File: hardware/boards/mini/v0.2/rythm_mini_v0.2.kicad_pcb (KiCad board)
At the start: 8 copper layers, 18 x 50 mm, 73 parts, among them IC1 NAU88C22YG, IC2 IS42S32160F-6BLI, Q1 PMV37EN22, U1 W25Q128JVP, U2 LTV-217-G, U4 STM32H750XBHx, Y1 Crystal_GND24

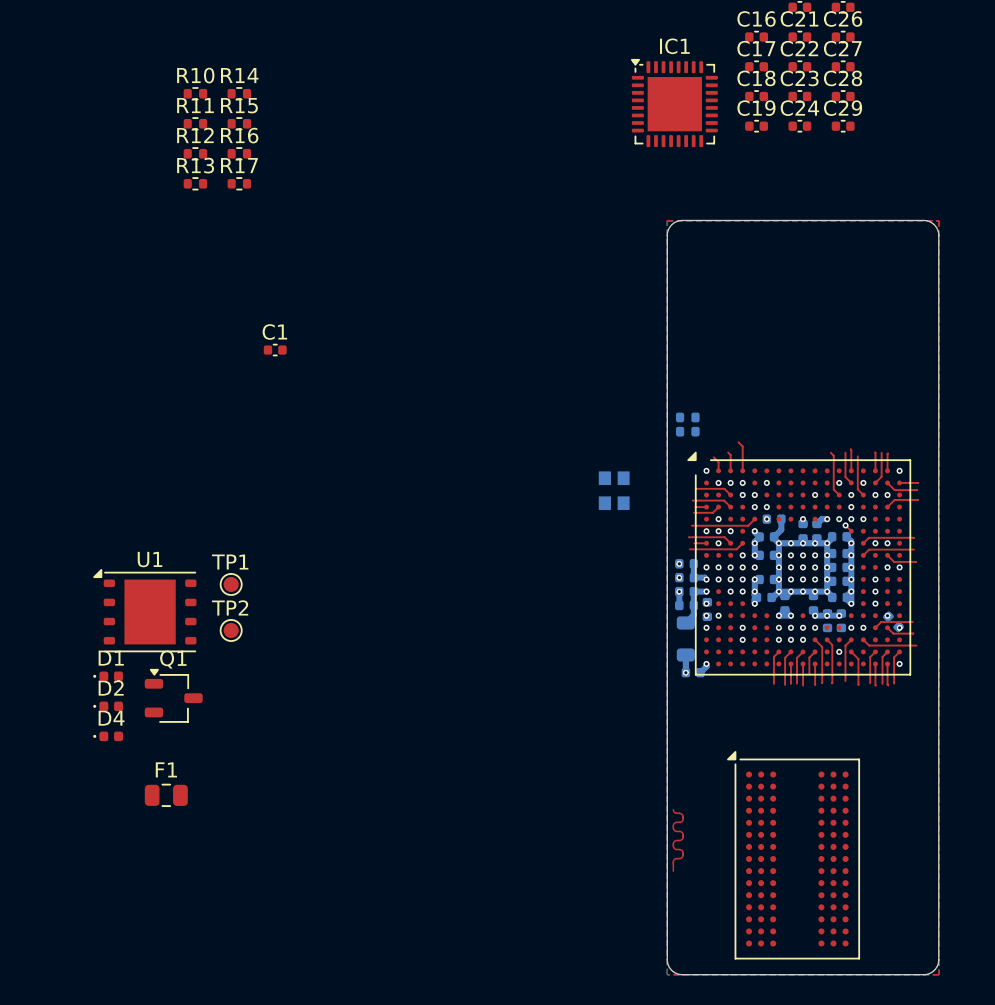
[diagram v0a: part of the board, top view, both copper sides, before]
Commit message: place stm32h750 decoupling capacitors
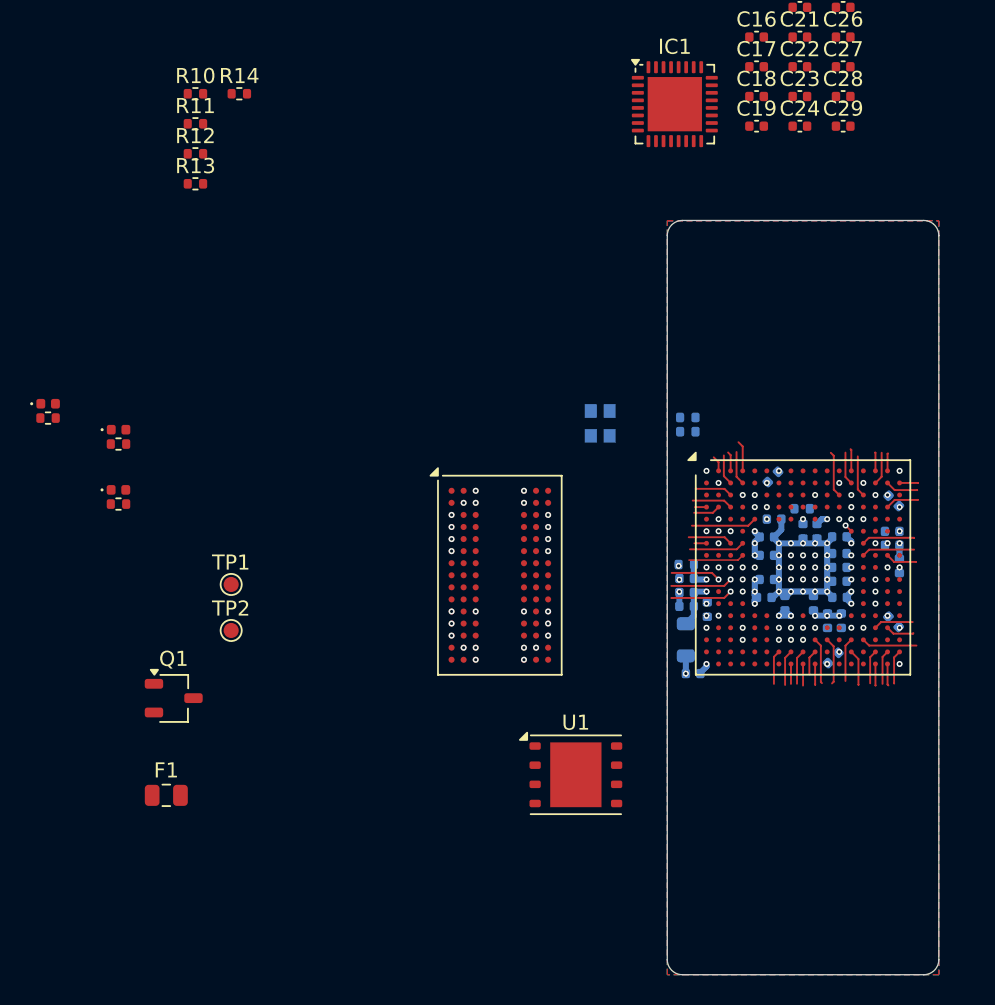
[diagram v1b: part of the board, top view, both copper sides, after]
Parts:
- added C2: 2.2 uF <100 mΩ ESR, Capacitor_SMD:C_0402_1005Metric, B.Cu at (86.0, 73.6)
- added C3: 2.2 uF <100 mΩ ESR, Capacitor_SMD:C_0402_1005Metric, B.Cu at (78.0, 72.0)
- added C4: 1uF 600mΩ, Capacitor_SMD:C_0402_1005Metric, B.Cu at (85.9, 75.6)
- added C5: 100nF, Capacitor_SMD:C_0402_1005Metric, B.Cu at (85.9, 76.5)
- added C6: 1uF, Capacitor_SMD:C_0402_1005Metric, B.Cu at (86.4, 77.9)
- added R18: 10k, Resistor_SMD:R_0402_1005Metric, B.Cu at (79.9, 74.1)
- C1: moved to B.Cu
- R5: value 4.7k -> 10k; footprint Capacitor_SMD:C_0402_1005Metric -> Resistor_SMD:R_0402_1005Metric
- moved C1 42.2 mm to (82.0, 84.0), turned to 45 degrees
- moved U1 30.2 mm to (64.9, 91.7)
- moved IC2 27.3 mm to (59.9, 78.5)
- moved R17 22.7 mm to (34.6, 73.8)
- moved R15 22.7 mm to (34.6, 69.8)
- moved R16 21.6 mm to (29.9, 68.1)
- moved D1 18.5 mm to (30.0, 67.2)
- moved D2 18.3 mm to (34.6, 68.9)
- moved D4 16.3 mm to (34.6, 72.9)
- moved Y1 4.56 mm to (66.6, 68.5)
- moved C31 0.06 mm to (72.3, 80.6)
- moved C30 0.06 mm to (72.3, 79.7)
- moved C32 0.06 mm to (72.7, 85.0)
- moved C33 0.06 mm to (72.3, 78.7)
- moved FB1 0.06 mm to (72.2, 82.8)
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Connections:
- C1 pad 1: unconnected-(C1-Pad1) -> Net-(C1-Pad1)
- C1 pad 2: unconnected-(C1-Pad2) -> GND
- U4 pad A7: unconnected-(U4L-VCAP-PadA7) -> Net-(C3-Pad1)
- U4 pad D17: unconnected-(U4L-VCAP-PadD17) -> Net-(C2-Pad1)
- U4 pad E7: unconnected-(U4L-PDR_ON-PadE7) -> +3.3V
- U4 pad E8: unconnected-(U4L-BOOT0-PadE8) -> /BOOT0
- U4 pad F17: unconnected-(U4L-VDD33_USB-PadF17) -> +3.3V
- U4 pad G17: unconnected-(U4L-VDD50_USB-PadG17) -> +3.3V
- U4 pad U11: unconnected-(U4L-VCAP-PadU11) -> Net-(C1-Pad1)
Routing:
- net +3.3V: track 17.3 -> 35.9 mm, vias 23 -> 39
- net /FMC_A4: track 0.00 -> 5.41 mm
- net /FMC_A5: track 0.00 -> 4.78 mm
- net /FMC_D6: track 0.00 -> 4.44 mm
- net /FMC_D8: track 0.00 -> 4.32 mm
- net /QSPI_CLK: track 0.00 -> 4.11 mm
- net /QSPI_IO2: track 0.00 -> 4.11 mm
- net /FMC_A7: track 0.00 -> 3.97 mm
- net /FMC_A8: track 0.00 -> 3.96 mm
- net /I2C_SCL: track 0.00 -> 3.96 mm
- net /FMC_A3: track 0.00 -> 3.70 mm, vias 1 -> 0
- net /FMC_A6: track 0.00 -> 3.63 mm
- net /I2C_SDA: track 0.00 -> 3.50 mm
- net /QSPI_IO3: track 6.62 -> 3.29 mm
- net /FMC_NBL0: track 0.00 -> 3.31 mm
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
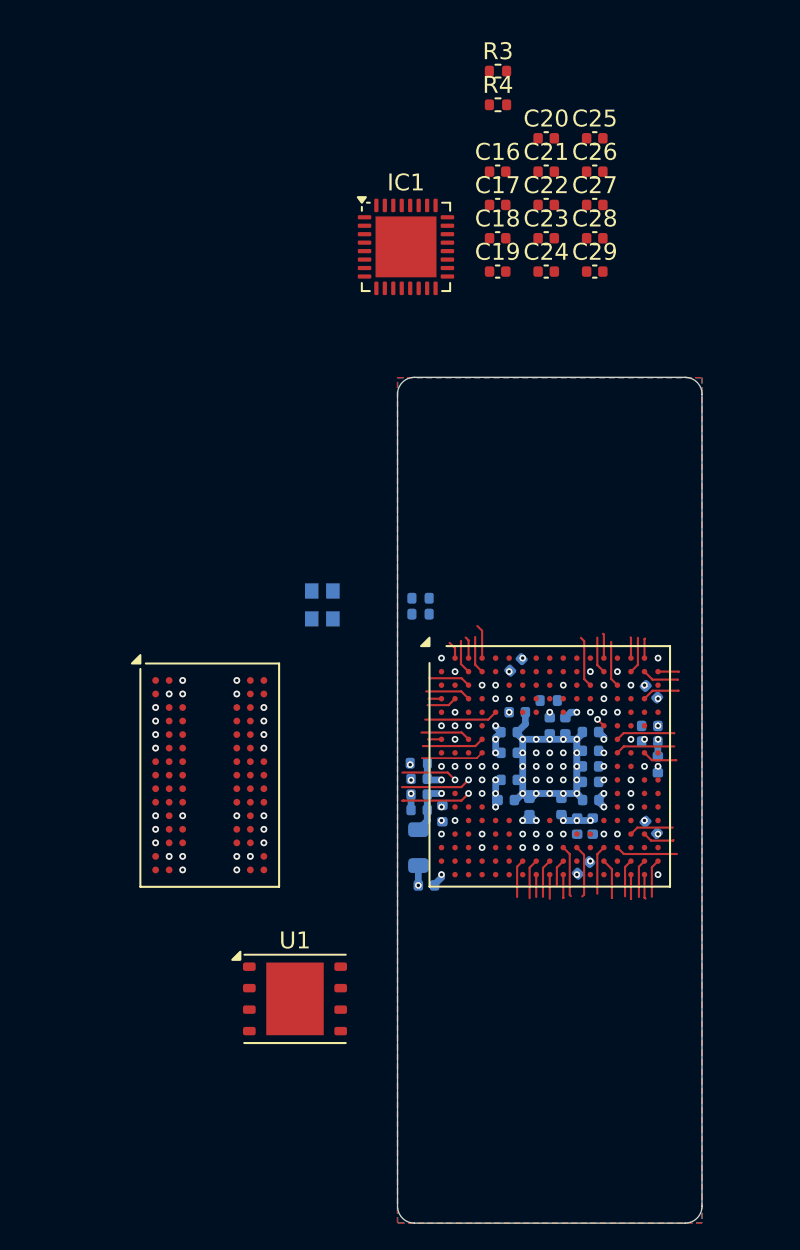
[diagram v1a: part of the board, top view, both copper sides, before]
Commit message: mini: more SDRAM routing work
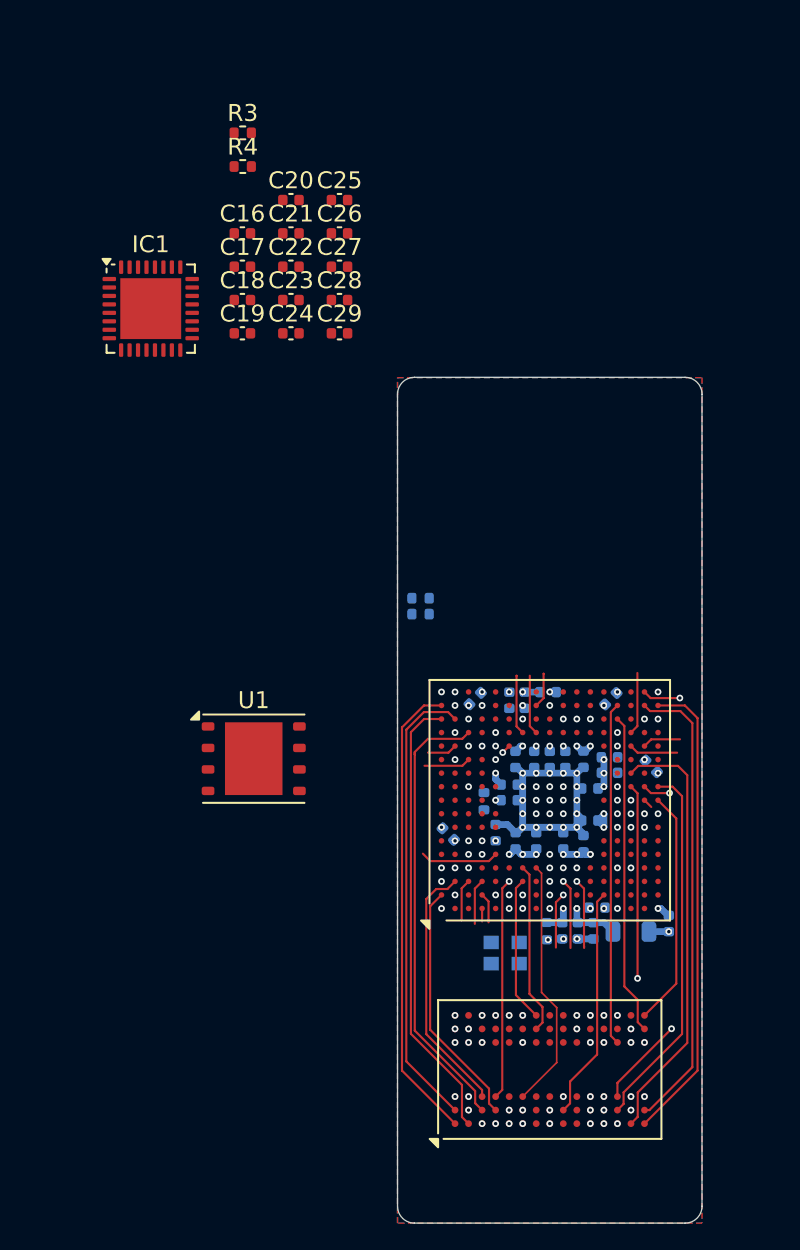
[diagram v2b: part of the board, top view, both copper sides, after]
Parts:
- moved IC2 26.6 mm to (80.0, 95.9), turned to 90 degrees
- moved Y1 23.2 mm to (77.4, 89.0), turned to 90 degrees
- moved C20 15.5 mm to (64.7, 44.5)
- moved C25 15.5 mm to (67.6, 44.5)
- moved C16 15.5 mm to (61.8, 46.5)
- moved C17 15.5 mm to (61.8, 48.5)
- moved C18 15.5 mm to (61.8, 50.4)
- moved C19 15.5 mm to (61.8, 52.4)
- moved C21 15.5 mm to (64.7, 46.5)
- moved C22 15.5 mm to (64.7, 48.5)
- moved C23 15.5 mm to (64.7, 50.4)
- moved C24 15.5 mm to (64.7, 52.4)
- moved C26 15.5 mm to (67.6, 46.5)
- moved C27 15.5 mm to (67.6, 48.5)
- moved C28 15.5 mm to (67.6, 50.4)
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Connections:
- IC2 pad A1: /FMC_D26 -> /FMC_D24
- IC2 pad A2: /FMC_D24 -> /FMC_D26
- IC2 pad A8: /FMC_D23 -> /FMC_D21
- IC2 pad A9: /FMC_D21 -> /FMC_D23
- IC2 pad B1: /FMC_D28 -> /FMC_D25
- IC2 pad C3: /FMC_D25 -> /FMC_D29
- IC2 pad D2: /FMC_D29 -> /FMC_D28
- IC2 pad N2: /FMC_D12 -> /FMC_D11
- IC2 pad P1: /FMC_D11 -> /FMC_D12
- IC2 pad P9: /FMC_D4 -> /FMC_D2
- IC2 pad R9: /FMC_D2 -> /FMC_D4
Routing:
- net /FMC_D13: track 1.44 -> 27.9 mm
- net /FMC_D24: track 1.17 -> 27.6 mm
- net /FMC_D14: track 2.24 -> 28.1 mm, vias 0 -> 2
- net /FMC_D25: track 1.23 -> 26.7 mm
- net /FMC_D15: track 2.26 -> 27.5 mm
- net /FMC_D22: track 1.23 -> 26.4 mm, vias 0 -> 2
- net /FMC_D26: track 2.17 -> 27.2 mm
- net /FMC_D27: track 2.71 -> 26.6 mm
- net /FMC_D12: track 3.11 -> 25.7 mm
- net /FMC_D21: track 2.21 -> 24.5 mm, vias 0 -> 2
- net /FMC_D10: track 1.66 -> 23.0 mm, vias 0 -> 2
- net /FMC_D11: track 1.38 -> 21.8 mm
- net /FMC_D23: track 2.17 -> 21.3 mm, vias 0 -> 2
- net /FMC_D0: track 1.89 -> 20.2 mm
- net /FMC_D1: track 2.63 -> 19.0 mm
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
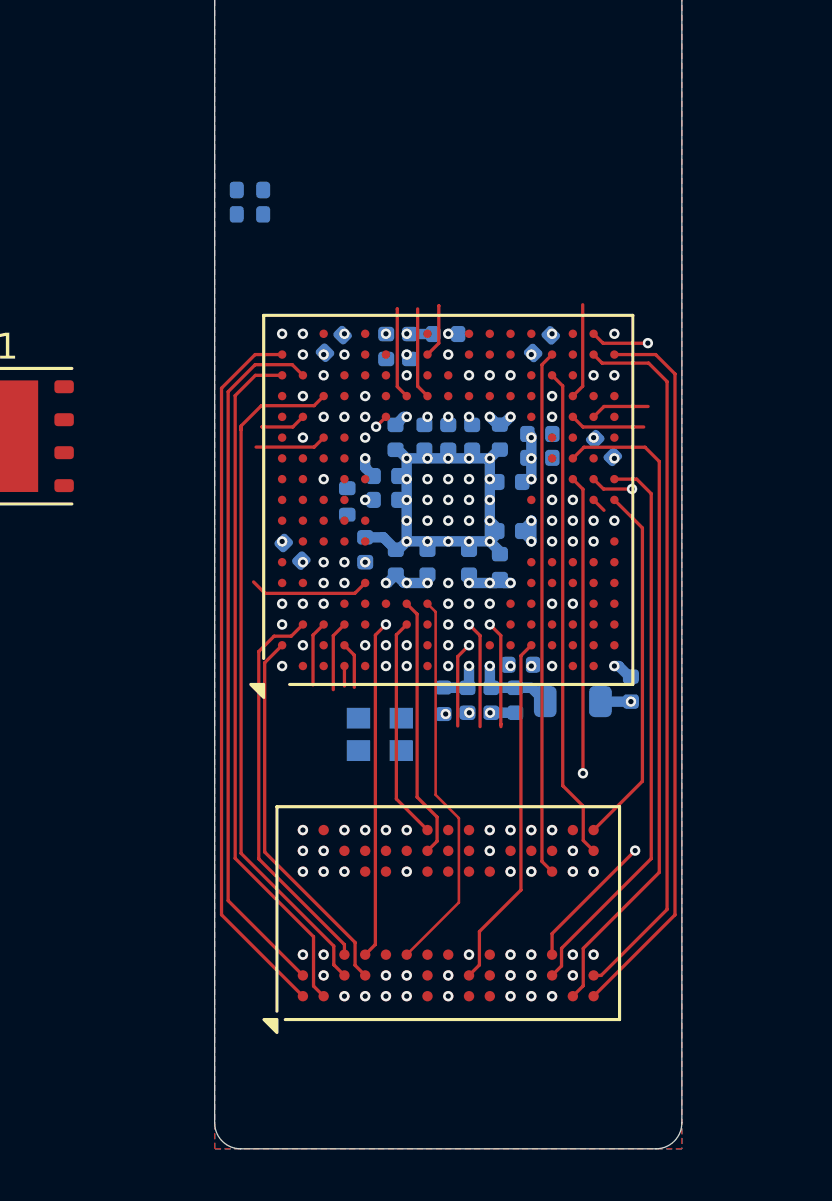
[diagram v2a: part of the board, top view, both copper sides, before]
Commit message: second mini SDRAM routing attempt
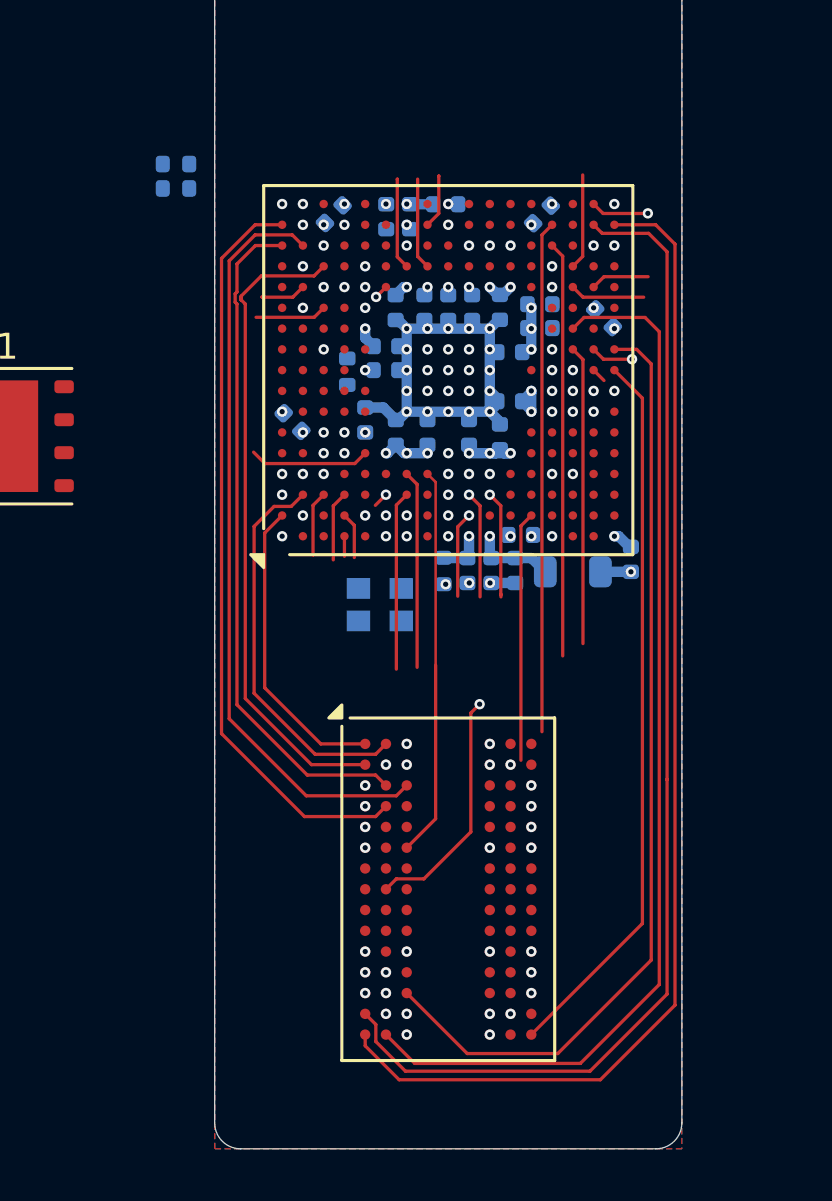
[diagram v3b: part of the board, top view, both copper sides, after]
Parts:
- moved C1 5.00 mm to (86.0, 73.0)
- moved C15 5.00 mm to (82.8, 81.3)
- moved C2 5.00 mm to (75.6, 69.0)
- moved C3 5.00 mm to (74.0, 77.0)
- moved C30 5.00 mm to (81.7, 82.7)
- moved C31 5.00 mm to (82.6, 82.7)
- moved C32 5.00 mm to (87.0, 82.3)
- moved C33 5.00 mm to (80.7, 82.7)
- moved C4 5.00 mm to (77.6, 69.1)
- moved C48 5.00 mm to (83.5, 72.5)
- moved C5 5.00 mm to (78.5, 69.1)
- moved C50 5.00 mm to (82.0, 72.6)
- moved C51 5.00 mm to (78.0, 72.6)
- moved C52 5.00 mm to (82.0, 77.6)
- moved C54 5.00 mm to (83.5, 73.4)
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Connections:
- IC2 pad A1: /FMC_D24 -> /FMC_D28
- IC2 pad A2: /FMC_D26 -> /FMC_D29
- IC2 pad B1: /FMC_D25 -> /FMC_D27
- IC2 pad C2: /FMC_D27 -> /FMC_D25
- IC2 pad C3: /FMC_D29 -> /FMC_D26
- IC2 pad D2: /FMC_D28 -> /FMC_D24
- IC2 pad N2: /FMC_D11 -> /FMC_D14
- IC2 pad N3: /FMC_D14 -> /FMC_D11
- IC2 pad P1: /FMC_D12 -> /FMC_D15
- IC2 pad R2: /FMC_D15 -> /FMC_D12
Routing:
- net /FMC_D15: track 27.5 -> 46.0 mm
- net /FMC_D13: track 27.9 -> 46.1 mm
- net /FMC_D12: track 25.7 -> 41.1 mm
- net /FMC_D11: track 21.8 -> 36.5 mm
- net /FMC_D4: track 13.9 -> 27.8 mm
- net /FMC_D14: track 28.1 -> 41.9 mm
- net /FMC_D30: track 13.1 -> 0.55 mm, vias 2 -> 1
- net /FMC_D31: track 13.1 -> 0.58 mm
- net /FMC_D10: track 23.0 -> 34.7 mm
- net /FMC_D9: track 19.3 -> 11.5 mm, vias 2 -> 0
- net /FMC_D22: track 26.4 -> 20.4 mm, vias 2 -> 1
- net /FMC_A7: track 19.2 -> 14.0 mm, vias 2 -> 1
- net /FMC_A9: track 19.5 -> 14.4 mm, vias 2 -> 1
- net /FMC_A2: track 8.26 -> 13.3 mm
- net /FMC_D21: track 24.5 -> 20.2 mm, vias 2 -> 1
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
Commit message: implement sine oscillator and example
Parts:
- added U5: MT48LC32M8A2TG, Package_SO:TSOP-II-54_22.2x10.16mm_P0.8mm, F.Cu at (6.79, 11.4)
- moved R2 8.42 mm to (61.4, 65.0)
- moved R1 8.42 mm to (61.4, 65.9)
- moved U1 8.42 mm to (54.4, 75.4)
- moved IC2 1.00 mm to (80.0, 94.0)
- moved C1 0.06 mm to (86.0, 72.9)
- moved C6 0.06 mm to (79.9, 68.5)
- moved C61 0.06 mm to (82.3, 74.2)
- moved C67 0.06 mm to (82.3, 76.1)
- moved C69 0.06 mm to (78.0, 77.3)
- moved C3 0.06 mm to (74.0, 76.9)
- moved C30 0.06 mm to (81.6, 82.7)
- moved C31 0.06 mm to (82.6, 82.7)
- moved C32 0.06 mm to (87.0, 82.2)
- moved C33 0.06 mm to (80.7, 82.7)
- moved C4 0.06 mm to (77.6, 69.0)
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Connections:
- IC2 pad N2: /FMC_D14 -> /FMC_D12
- IC2 pad N7: /FMC_D0 -> /FMC_D1
- IC2 pad P1: /FMC_D15 -> /FMC_D13
- IC2 pad R1: /FMC_D13 -> /FMC_D14
- IC2 pad R2: /FMC_D12 -> /FMC_D15
- IC2 pad R8: /FMC_D1 -> /FMC_D0
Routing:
- net /FMC_D10: track 34.7 -> 0.00 mm
- net /FMC_D5: track 0.57 -> 28.5 mm, vias 0 -> 2
- net /FMC_A8: track 22.5 -> 0.00 mm, vias 2 -> 1
- net /FMC_D1: track 16.0 -> 38.2 mm, vias 0 -> 2
- net /FMC_A10: track 0.00 -> 21.5 mm
- net /FMC_A11: track 0.00 -> 20.7 mm, vias 1 -> 0
- net /FMC_D22: track 20.4 -> 0.00 mm, vias 1 -> 0
- net /FMC_D21: track 20.2 -> 0.00 mm, vias 1 -> 0
- net /FMC_SDNRAS: track 0.00 -> 19.7 mm, vias 1 -> 2
- net /FMC_D0: track 19.7 -> 38.5 mm, vias 0 -> 2
- net /FMC_D23: track 17.7 -> 0.00 mm, vias 1 -> 0
- net /FMC_NBL3: track 0.00 -> 15.7 mm, vias 1 -> 2
- net /FMC_A3: track 15.0 -> 0.00 mm
- net /FMC_A9: track 14.4 -> 0.00 mm
- net /FMC_A7: track 14.0 -> 0.00 mm
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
